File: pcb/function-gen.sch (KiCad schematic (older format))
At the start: 53 parts, among them CON1 AVR-ISP-6, J1 USB-MINI-B, P1 CONN_2, P2 BNC, P3 CONN_8, P5 BNC, U1 LM1117-5V, U2 AT90USB162, U3 AD9833, U4 OPA357-SOT23-6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

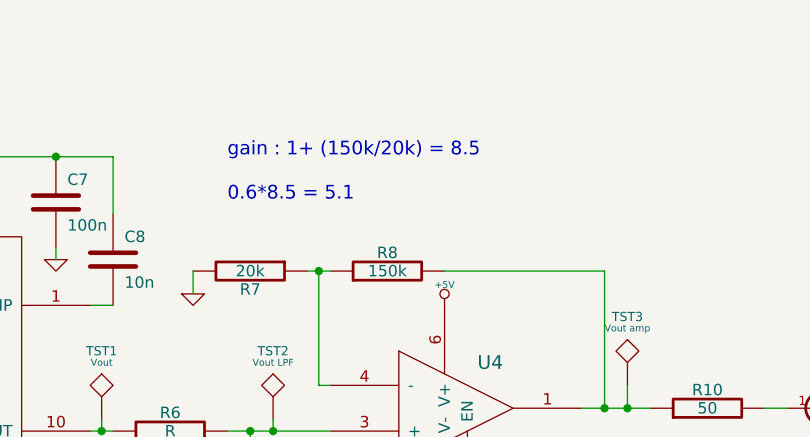
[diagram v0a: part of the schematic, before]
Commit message: changed opamp feedback resistors
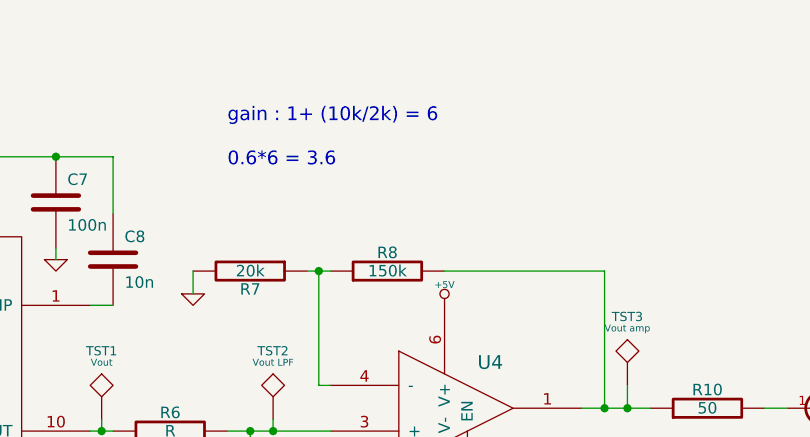
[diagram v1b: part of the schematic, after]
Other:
- note added: "gain : 1+ (10k/2k) = 6\n\n0.6*6 = 3.6\n"
- note removed: "gain : 1+ (150k/20k) = 8.5\n\n0.6*8.5 = 5.1\n"
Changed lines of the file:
@@
-EESchema Schematic File Version 2  date Thu 14 Jun 2012 09:57:22 PM EEST
+EESchema Schematic File Version 2  date Thu 21 Jun 2012 01:48:41 AM EEST
 LIBS:power
 LIBS:device
@@
 Sheet 1 1
 Title ""
-Date "14 jun 2012"
+Date "20 jun 2012"
 Rev ""
 Comp ""
@@
 Comment4 ""
 $EndDescr
-Text Notes 7000 1450 0    60   ~ 0
-gain : 1+ (150k/20k) = 8.5\n\n0.6*8.5 = 5.1\n
+Text Notes 7000 1300 0    60   ~ 0
+gain : 1+ (10k/2k) = 6\n\n0.6*6 = 3.6\n
 Wire Wire Line
 	8000 5550 8500 5550

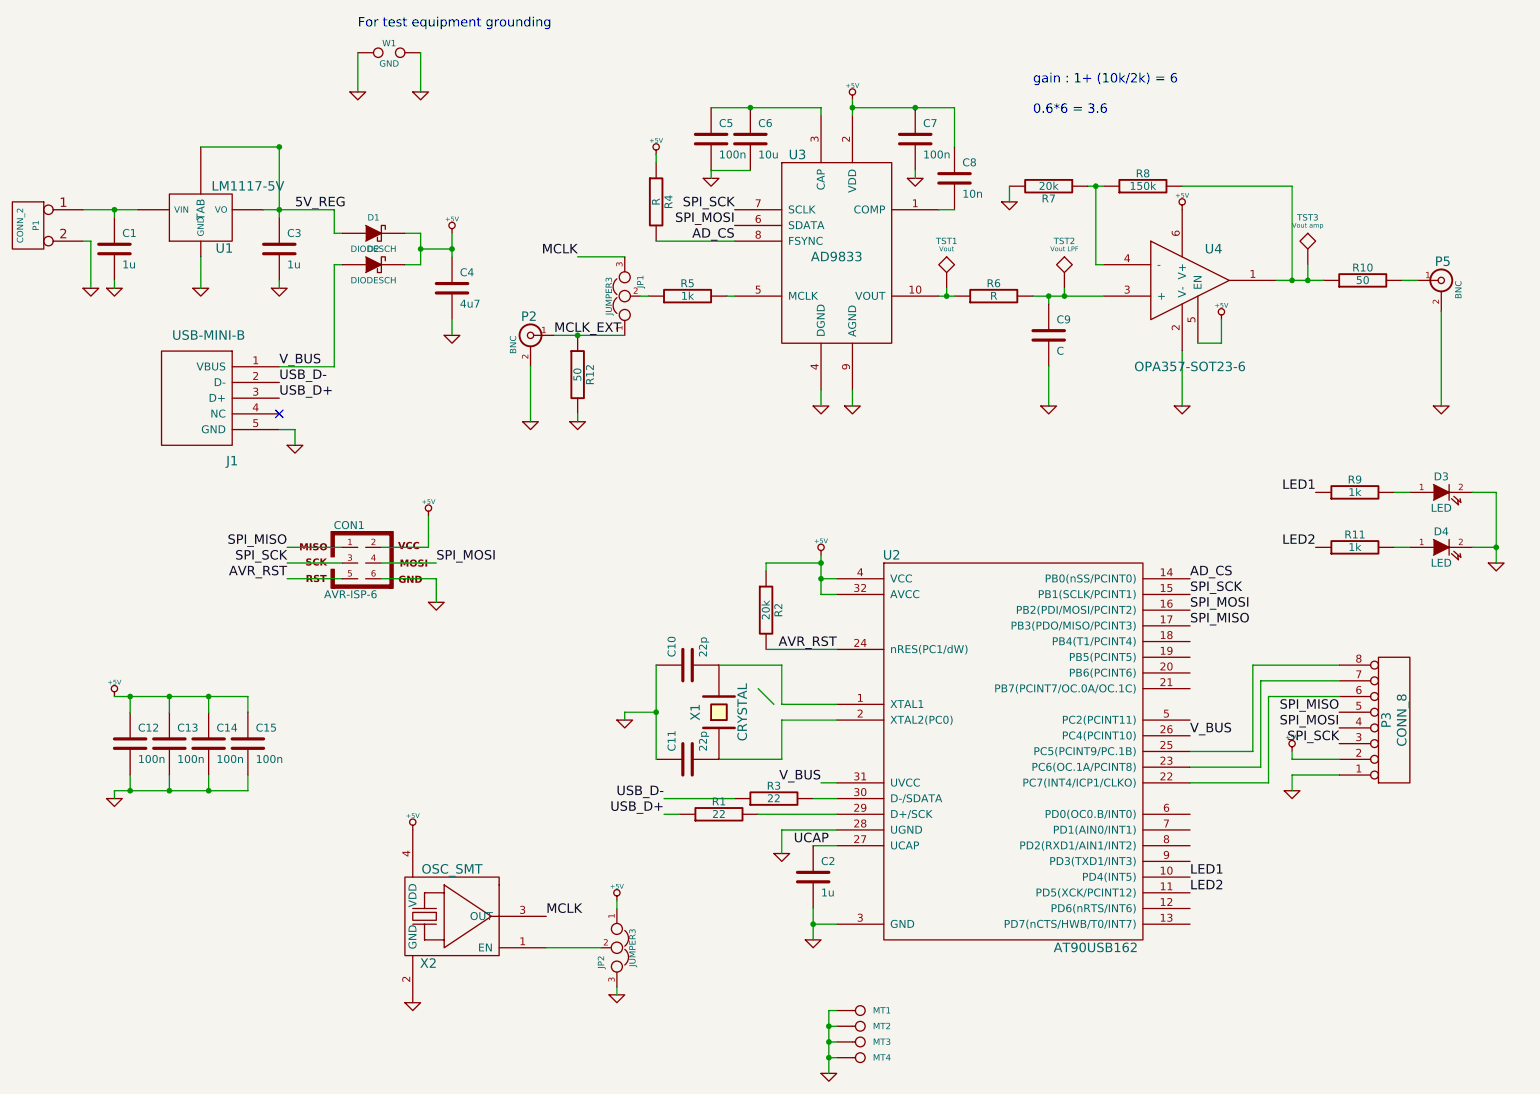
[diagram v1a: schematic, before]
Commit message: PCB change, AVR-VBUS connected to +5V, not to USB
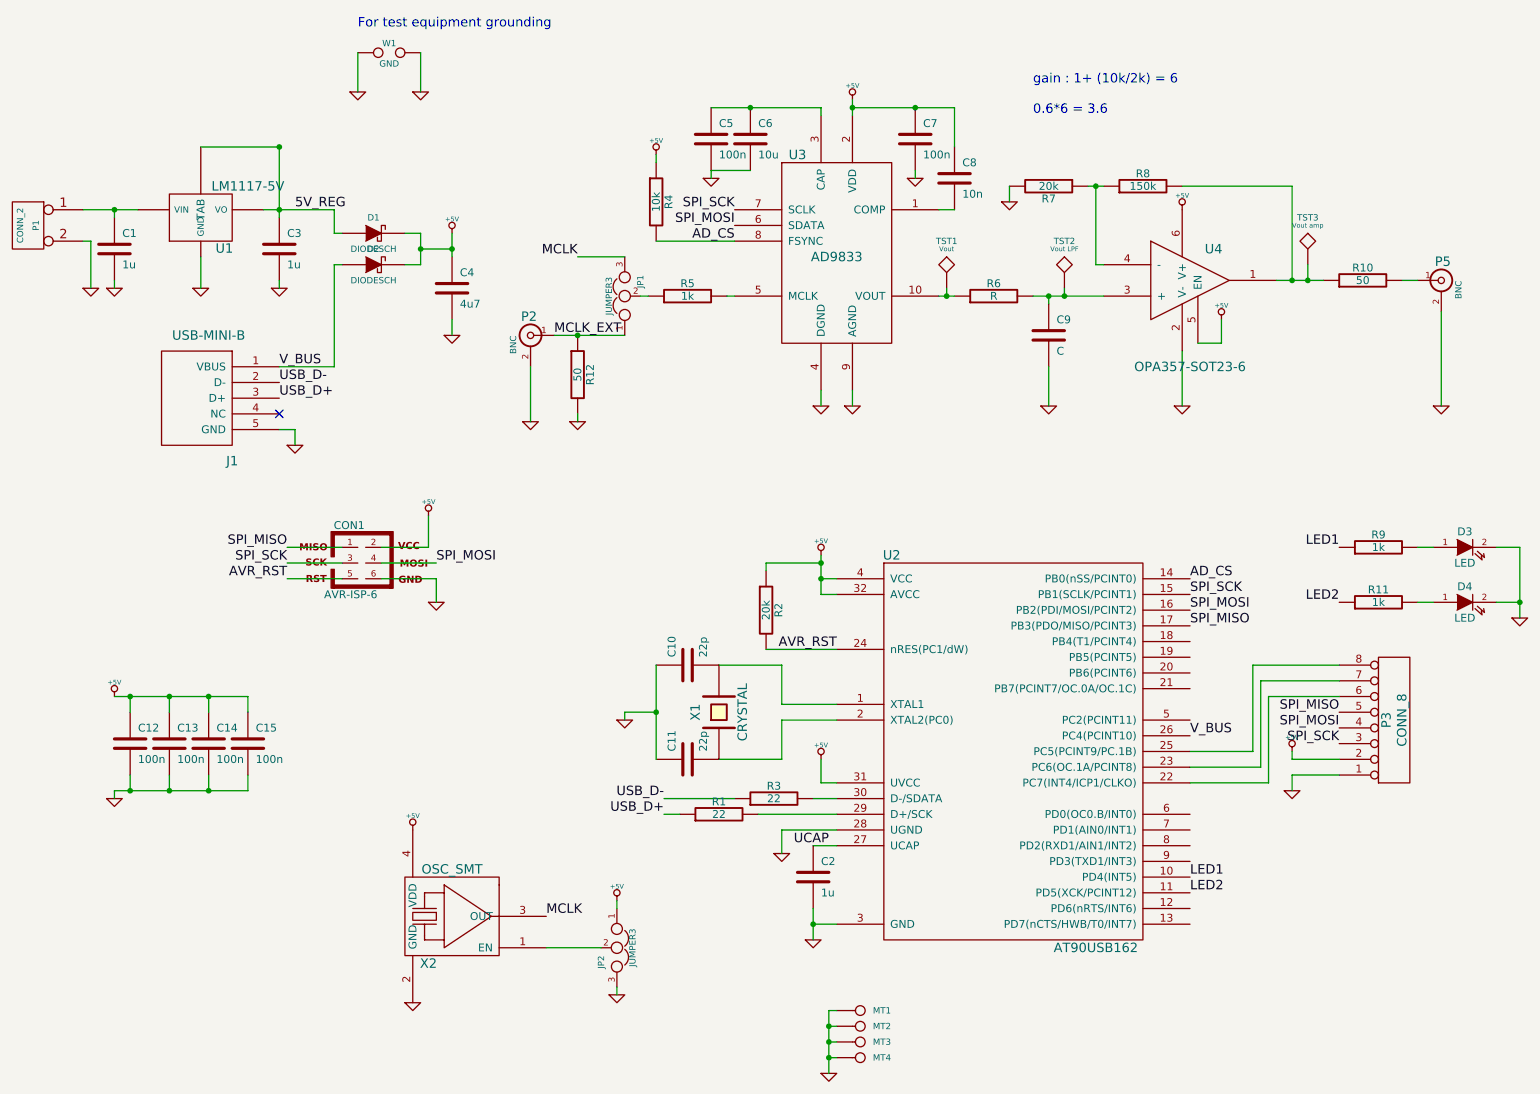
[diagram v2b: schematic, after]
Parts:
- R4: value R -> 10k
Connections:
- net +5V: now also U2.31 (UVCC)
- net V_BUS: no longer U2.31 (UVCC)
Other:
- moved on the sheet: D3, D4, R11, R9
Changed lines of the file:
@@
-EESchema Schematic File Version 2  date Thu 21 Jun 2012 01:48:41 AM EEST
+EESchema Schematic File Version 2  date Fri Aug 10 18:49:11 2012
 LIBS:power
 LIBS:device
@@
 EELAYER 25  0
 EELAYER END
-$Descr A4 11700 8267
+$Descr A4 11693 8268
 encoding utf-8
 Sheet 1 1
 Title ""
-Date "20 jun 2012"
+Date "10 aug 2012"
 Rev ""
 Comp ""
@@
 	8400 5350 8000 5350
 Wire Wire Line
-	9300 3700 9400 3700
-Wire Wire Line
-	9800 3700 9950 3700
-Wire Wire Line
-	9950 3700 9950 4150
+	9450 4050 9550 4050
+Wire Wire Line
+	9950 4050 10100 4050
+Wire Wire Line
+	10100 4050 10100 4500
 Wire Wire Line
 	4350 6900 4350 6850
@@
 	4350 6300 4350 6350
 Wire Wire Line
-	9800 4050 9950 4050
-Connection ~ 9950 4050
-Wire Wire Line
-	9300 4050 9400 4050
+	9950 4400 10100 4400
+Connection ~ 10100 4400
+Wire Wire Line
+	9450 4400 9550 4400
 Wire Wire Line
 	8000 5450 8450 5450
@@
 Text Label 8000 6150 0    60   ~ 0
 LED1
-Text Label 8800 4050 2    60   ~ 0
+Text Label 8950 4400 2    60   ~ 0
 LED2
-Text Label 8800 3700 2    60   ~ 0
+Text Label 8950 4050 2    60   ~ 0
 LED1
 $Comp
 L R R11
 U 1 1 4FD99A9B
-P 9050 4050
-F 0 "R11" V 9130 4050 50  0000 C CNN
-F 1 "1k" V 9050 4050 50  0000 C CNN
-	1    9050 4050
+P 9200 4400
+F 0 "R11" V 9280 4400 50  0000 C CNN
+F 1 "1k" V 9200 4400 50  0000 C CNN
+	1    9200 4400
 	0    -1   -1   0
 $EndComp
@@
 L R R9
 U 1 1 4FD99A98
-P 9050 3700
-F 0 "R9" V 9130 3700 50  0000 C CNN
-F 1 "1k" V 9050 3700 50  0000 C CNN
-	1    9050 3700
+P 9200 4050
+F 0 "R9" V 9280 4050 50  0000 C CNN
+F 1 "1k" V 9200 4050 50  0000 C CNN
+	1    9200 4050
 	0    -1   -1   0
 $EndComp
@@
 L GND #PWR01
 U 1 1 4FD99A94
-P 9950 4150
-F 0 "#PWR01" H 9950 4150 30  0001 C CNN
-F 1 "GND" H 9950 4080 30  0001 C CNN
-	1    9950 4150
+P 10100 4500
+F 0 "#PWR01" H 10100 4500 30  0001 C CNN
+F 1 "GND" H 10100 4430 30  0001 C CNN
+	1    10100 4500
 	1    0    0    -1
 $EndComp
@@
 L LED D4
 U 1 1 4FD99A87
-P 9600 4050
-F 0 "D4" H 9600 4150 50  0000 C CNN
-F 1 "LED" H 9600 3950 50  0000 C CNN
-	1    9600 4050
+P 9750 4400
+F 0 "D4" H 9750 4500 50  0000 C CNN
+F 1 "LED" H 9750 4300 50  0000 C CNN
+	1    9750 4400
 	1    0    0    -1
 $EndComp
@@
 L LED D3
 U 1 1 4FD99A85
-P 9600 3700
-F 0 "D3" H 9600 3800 50  0000 C CNN
-F 1 "LED" H 9600 3600 50  0000 C CNN
-	1    9600 3700
+P 9750 4050
+F 0 "D3" H 9750 4150 50  0000 C CNN
+F 1 "LED" H 9750 3950 50  0000 C CNN
+	1    9750 4050
 	1    0    0    -1
 $EndComp
@@
 	1    0    0    -1
 $EndComp
-Entry Wire Line
-	5250 4950 5350 5050
-Text Label 5650 5550 2    60   ~ 0
-V_BUS
 Text Label 8950 5100 2    60   ~ 0
 SPI_MISO
@@
 P 4600 1850
 F 0 "R4" V 4680 1850 50  0000 C CNN
-F 1 "R" V 4600 1850 50  0000 C CNN
+F 1 "10k" V 4600 1850 50  0000 C CNN
 	1    4600 1850
 	1    0    0    -1
@@
 	1    0    0    -1
 $EndComp
+$Comp
+L +5V #PWR040
+U 1 1 50253018
+P 5650 5400
+F 0 "#PWR040" H 5650 5490 20  0001 C CNN
+F 1 "+5V" H 5650 5490 30  0000 C CNN
+	1    5650 5400
+	1    0    0    -1
+$EndComp
+Wire Wire Line
+	5650 5400 5650 5550
 $EndSCHEMATC
